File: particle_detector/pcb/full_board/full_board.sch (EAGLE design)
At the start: 42 parts, among them IC1 LT1807R, IC2 TLV3501, IC3 LT3461, IC4 TEENSY 3.2, IC5 SENSL-SIPM

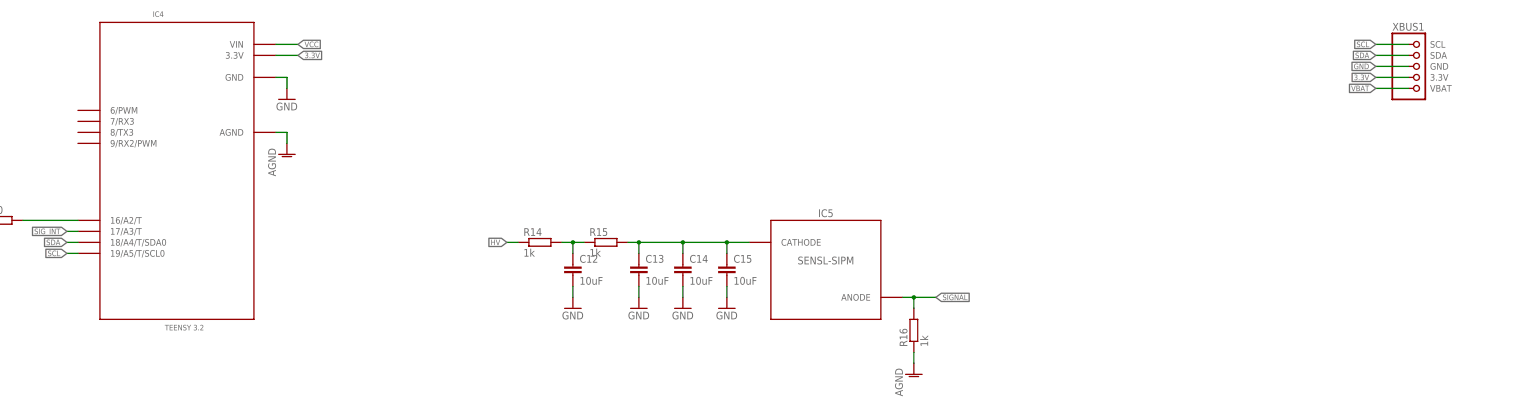
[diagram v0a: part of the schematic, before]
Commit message: finish full board; still needs Serial connnections (sent to PCBWay 2019.05.19)
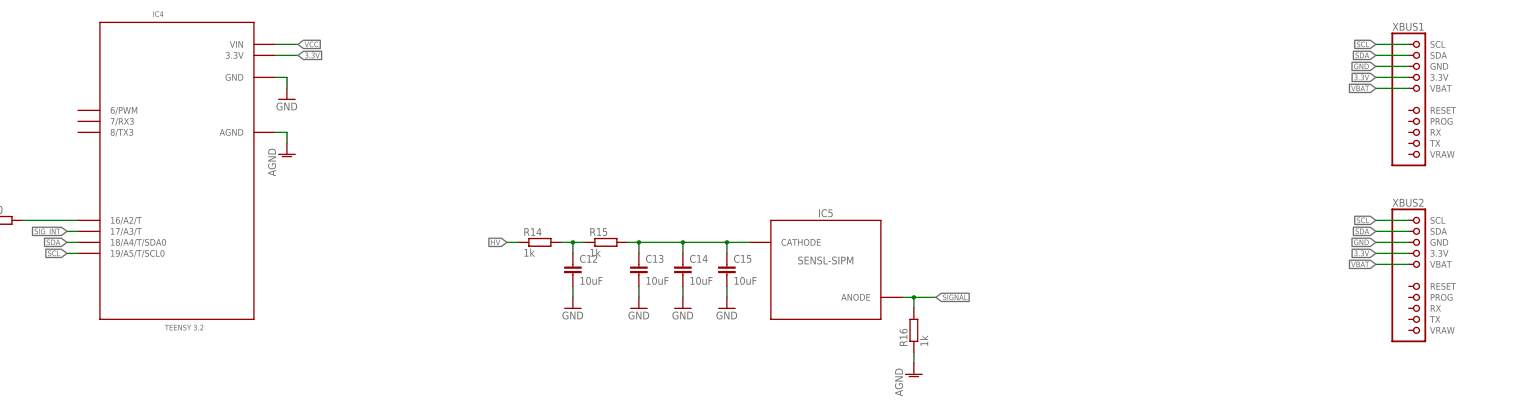
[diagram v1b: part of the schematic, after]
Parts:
- added XBUS2: (no value), personal:XINABOX-XBUS
- IC4: device personal:TEENSY_3.2_FOR_THINSAT -> personal:TEENSY_3.2_THINSAT
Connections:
- net 3.3V: now also XBUS2.3.3V
- net GND: now also XBUS2.GND
- net SCL: now also XBUS2.SCL
- net SDA: now also XBUS2.SDA
- net VBAT: now also XBUS2.VBAT

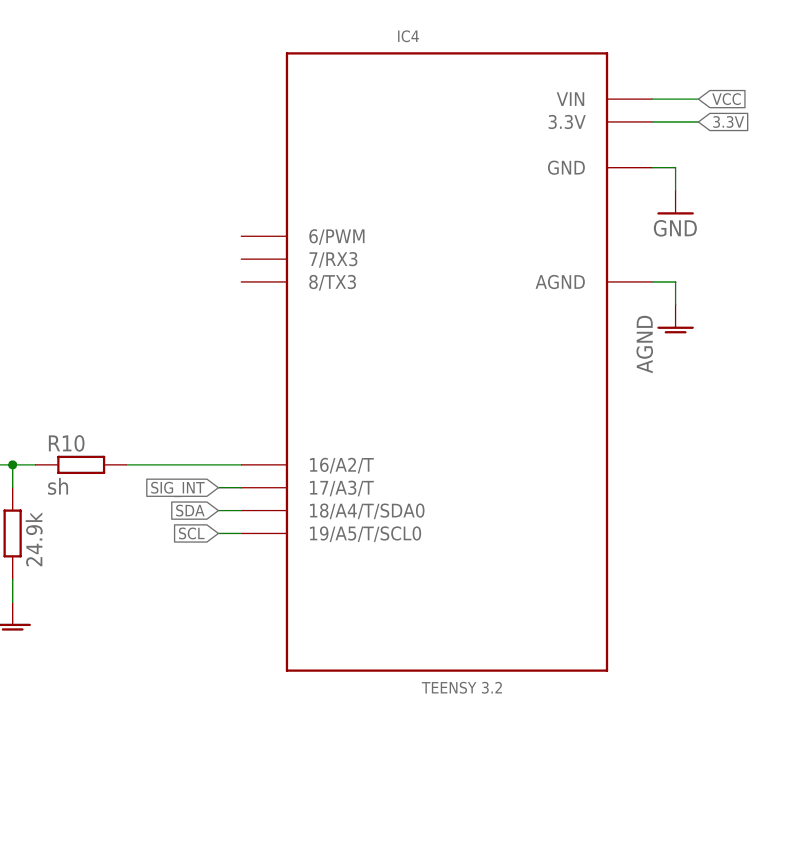
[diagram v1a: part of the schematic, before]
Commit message: remove empty xbus header, add TX/RX pins to teensy
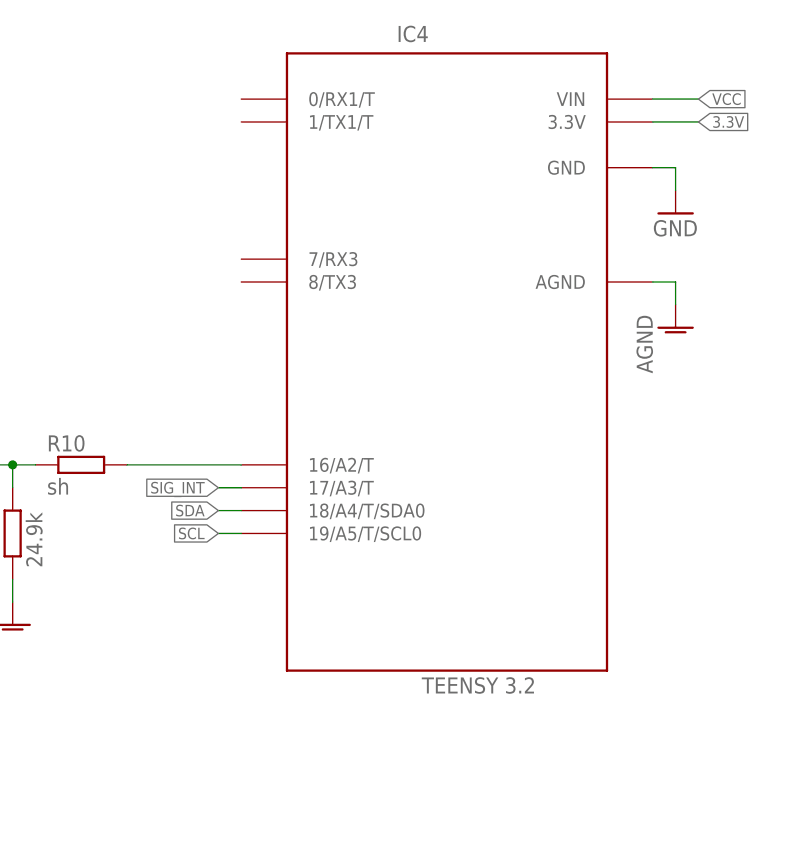
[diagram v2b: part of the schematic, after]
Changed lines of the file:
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@@
 </instance>
 <instance part="IC4" gate="G$1" x="86.36" y="218.44" smashed="yes">
-<attribute name="NAME" x="80.772" y="252.73" size="1.27" layer="95" font="vector" ratio="15"/>
-<attribute name="VALUE" x="83.566" y="180.34" size="1.27" layer="96" font="vector" ratio="15"/>
+<attribute name="NAME" x="80.772" y="252.73" size="1.778" layer="95"/>
+<attribute name="VALUE" x="83.566" y="180.34" size="1.778" layer="96"/>
 </instance>
 <instance part="GND22" gate="VR1" x="38.1" y="187.96" smashed="yes">

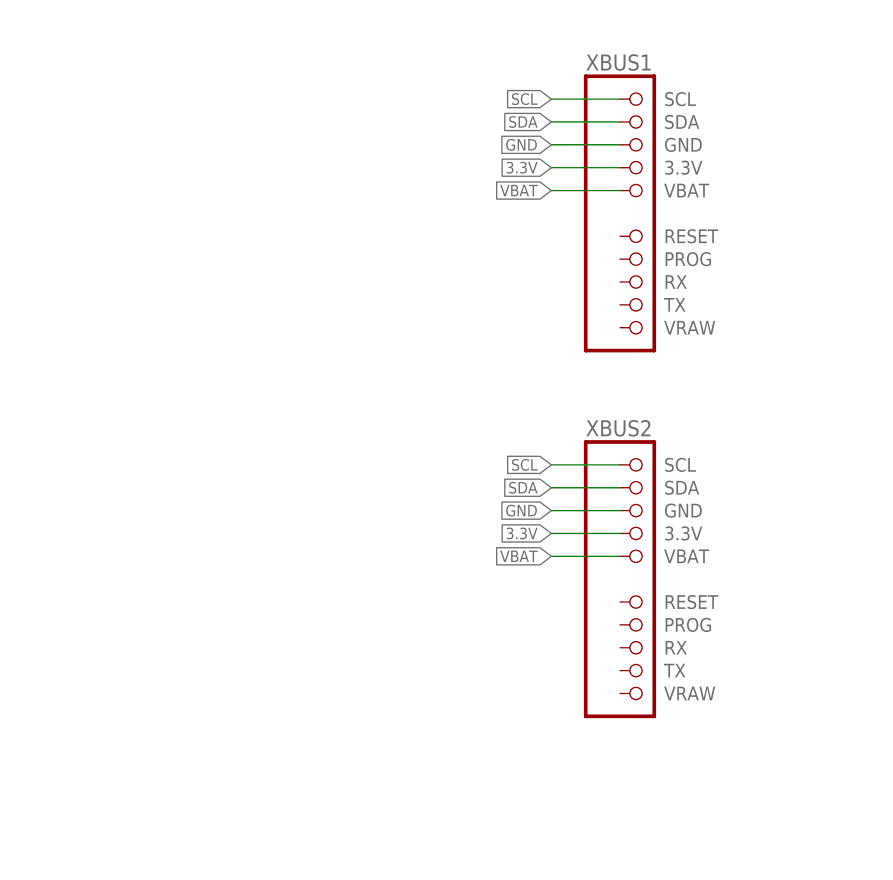
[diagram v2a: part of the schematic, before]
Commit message: swap teensy for new teensy pinout with TX/RX
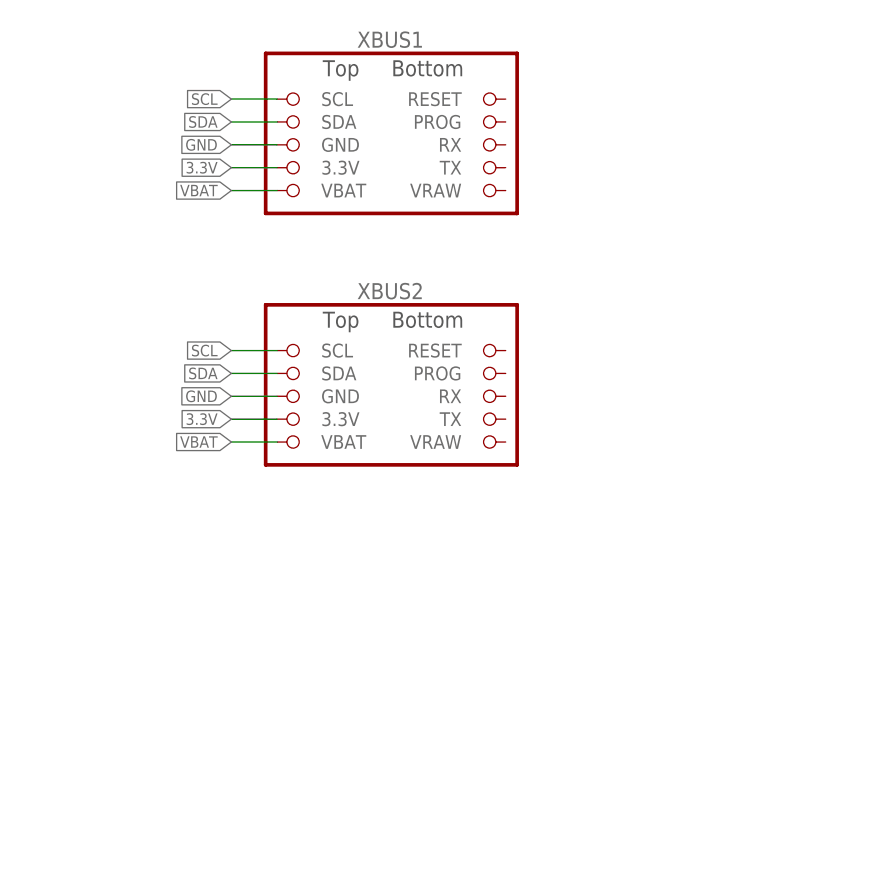
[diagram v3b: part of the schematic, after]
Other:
- note added: "Xinabox Headers"
- note removed: "I2C and Xinabox Header"
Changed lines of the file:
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@@
 <wire x1="276.86" y1="162.56" x2="276.86" y2="220.98" width="0.1524" layer="98" style="shortdash"/>
 <wire x1="276.86" y1="220.98" x2="152.4" y2="220.98" width="0.1524" layer="98" style="shortdash"/>
-<wire x1="312.42" y1="261.62" x2="386.08" y2="261.62" width="0.1524" layer="98" style="shortdash"/>
-<wire x1="386.08" y1="261.62" x2="386.08" y2="162.56" width="0.1524" layer="98" style="shortdash"/>
-<wire x1="386.08" y1="162.56" x2="312.42" y2="162.56" width="0.1524" layer="98" style="shortdash"/>
-<wire x1="312.42" y1="162.56" x2="312.42" y2="261.62" width="0.1524" layer="98" style="shortdash"/>
+<wire x1="312.42" y1="261.62" x2="370.84" y2="261.62" width="0.1524" layer="98" style="shortdash"/>
+<wire x1="370.84" y1="261.62" x2="370.84" y2="200.66" width="0.1524" layer="98" style="shortdash"/>
+<wire x1="370.84" y1="200.66" x2="312.42" y2="200.66" width="0.1524" layer="98" style="shortdash"/>
+<wire x1="312.42" y1="200.66" x2="312.42" y2="261.62" width="0.1524" layer="98" style="shortdash"/>
 <text x="210.82" y="215.9" size="2.54" layer="98" align="bottom-center">Detector</text>
-<text x="347.98" y="256.54" size="2.54" layer="98" align="bottom-center">I2C and Xinabox Header</text>
+<text x="342.9" y="256.54" size="2.54" layer="98" align="bottom-center">Xinabox Headers</text>
 </plain>
 <instances>
@@
 <attribute name="VALUE" x="109.22" y="231.14" size="1.778" layer="96"/>
 </instance>
-<instance part="XBUS1" gate="G$1" x="373.38" y="241.3" smashed="yes">
-<attribute name="NAME" x="367.03" y="249.555" size="1.778" layer="95"/>
-<attribute name="VALUE" x="367.03" y="215.9" size="1.778" layer="96"/>
+<instance part="XBUS1" gate="G$1" x="345.44" y="241.3" smashed="yes">
+<attribute name="NAME" x="341.63" y="252.095" size="1.778" layer="95"/>
+<attribute name="VALUE" x="339.09" y="215.9" size="1.778" layer="96"/>
 </instance>
 <instance part="AGND1" gate="VR1" x="111.76" y="220.98" smashed="yes">
@@
 <attribute name="VALUE" x="190.5" y="182.88" size="1.778" layer="96"/>
 </instance>
-<instance part="XBUS2" gate="G$1" x="373.38" y="200.66" smashed="yes">
-<attribute name="NAME" x="367.03" y="208.915" size="1.778" layer="95"/>
-<attribute name="VALUE" x="367.03" y="175.26" size="1.778" layer="96"/>
+<instance part="XBUS2" gate="G$1" x="345.44" y="213.36" smashed="yes">
+<attribute name="NAME" x="341.63" y="224.155" size="1.778" layer="95"/>
+<attribute name="VALUE" x="339.09" y="187.96" size="1.778" layer="96"/>
 </instance>
 </instances>
@@
 <segment>
 <pinref part="XBUS1" gate="G$1" pin="GND"/>
-<wire x1="370.84" y1="241.3" x2="363.22" y2="241.3" width="0.1524" layer="91"/>
-<label x="363.22" y="241.3" size="1.27" layer="95" rot="R180" xref="yes"/>
+<wire x1="332.74" y1="241.3" x2="327.66" y2="241.3" width="0.1524" layer="91"/>
+<label x="327.66" y="241.3" size="1.27" layer="95" rot="R180" xref="yes"/>
 </segment>
 <segment>
@@
 <segment>
 <pinref part="XBUS2" gate="G$1" pin="GND"/>
-<wire x1="370.84" y1="200.66" x2="363.22" y2="200.66" width="0.1524" layer="91"/>
-<label x="363.22" y="200.66" size="1.27" layer="95" rot="R180" xref="yes"/>
+<wire x1="332.74" y1="213.36" x2="327.66" y2="213.36" width="0.1524" layer="91"/>
+<label x="327.66" y="213.36" size="1.27" layer="95" rot="R180" xref="yes"/>
 </segment>
 </net>
@@
 <segment>
 <pinref part="XBUS1" gate="G$1" pin="SDA"/>
-<wire x1="370.84" y1="243.84" x2="363.22" y2="243.84" width="0.1524" layer="91"/>
-<label x="363.22" y="243.84" size="1.27" layer="95" rot="R180" xref="yes"/>
+<wire x1="332.74" y1="243.84" x2="327.66" y2="243.84" width="0.1524" layer="91"/>
+<label x="327.66" y="243.84" size="1.27" layer="95" rot="R180" xref="yes"/>
 </segment>
 <segment>
 <pinref part="XBUS2" gate="G$1" pin="SDA"/>
-<wire x1="370.84" y1="203.2" x2="363.22" y2="203.2" width="0.1524" layer="91"/>
-<label x="363.22" y="203.2" size="1.27" layer="95" rot="R180" xref="yes"/>
+<wire x1="332.74" y1="215.9" x2="327.66" y2="215.9" width="0.1524" layer="91"/>
+<label x="327.66" y="215.9" size="1.27" layer="95" rot="R180" xref="yes"/>
 </segment>
 </net>
@@
 <segment>
 <pinref part="XBUS1" gate="G$1" pin="SCL"/>
-<wire x1="370.84" y1="246.38" x2="363.22" y2="246.38" width="0.1524" layer="91"/>
-<label x="363.22" y="246.38" size="1.27" layer="95" rot="R180" xref="yes"/>
+<wire x1="332.74" y1="246.38" x2="327.66" y2="246.38" width="0.1524" layer="91"/>
+<label x="327.66" y="246.38" size="1.27" layer="95" rot="R180" xref="yes"/>
 </segment>
 <segment>
 <pinref part="XBUS2" gate="G$1" pin="SCL"/>
-<wire x1="370.84" y1="205.74" x2="363.22" y2="205.74" width="0.1524" layer="91"/>
-<label x="363.22" y="205.74" size="1.27" layer="95" rot="R180" xref="yes"/>
+<wire x1="332.74" y1="218.44" x2="327.66" y2="218.44" width="0.1524" layer="91"/>
+<label x="327.66" y="218.44" size="1.27" layer="95" rot="R180" xref="yes"/>
 </segment>
 </net>
@@
 <segment>
 <pinref part="XBUS1" gate="G$1" pin="3.3V"/>
-<wire x1="370.84" y1="238.76" x2="363.22" y2="238.76" width="0.1524" layer="91"/>
-<label x="363.22" y="238.76" size="1.27" layer="95" rot="R180" xref="yes"/>
+<wire x1="332.74" y1="238.76" x2="327.66" y2="238.76" width="0.1524" layer="91"/>
+<label x="327.66" y="238.76" size="1.27" layer="95" rot="R180" xref="yes"/>
 </segment>
 <segment>
@@
 <segment>
 <pinref part="XBUS2" gate="G$1" pin="3.3V"/>
-<wire x1="370.84" y1="198.12" x2="363.22" y2="198.12" width="0.1524" layer="91"/>
-<label x="363.22" y="198.12" size="1.27" layer="95" rot="R180" xref="yes"/>
+<wire x1="332.74" y1="210.82" x2="327.66" y2="210.82" width="0.1524" layer="91"/>
+<label x="327.66" y="210.82" size="1.27" layer="95" rot="R180" xref="yes"/>
 </segment>
 </net>
@@
 <segment>
 <pinref part="XBUS1" gate="G$1" pin="VBAT"/>
-<wire x1="370.84" y1="236.22" x2="363.22" y2="236.22" width="0.1524" layer="91"/>
-<label x="363.22" y="236.22" size="1.27" layer="95" rot="R180" xref="yes"/>
+<wire x1="332.74" y1="236.22" x2="327.66" y2="236.22" width="0.1524" layer="91"/>
+<label x="327.66" y="236.22" size="1.27" layer="95" rot="R180" xref="yes"/>
 </segment>
 <segment>
 <pinref part="XBUS2" gate="G$1" pin="VBAT"/>
-<wire x1="370.84" y1="195.58" x2="363.22" y2="195.58" width="0.1524" layer="91"/>
-<label x="363.22" y="195.58" size="1.27" layer="95" rot="R180" xref="yes"/>
-</segment>
-</net>
+<wire x1="332.74" y1="208.28" x2="327.66" y2="208.28" width="0.1524" layer="91"/>
+<label x="327.66" y="208.28" size="1.27" layer="95" rot="R180" xref="yes"/>
+</segment>
+</net>
